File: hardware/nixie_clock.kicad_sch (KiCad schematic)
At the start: 0 parts

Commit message: Update.
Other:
- sheet driver_3_digits_1_dot_right: file driver_3_digits_1_dot.kicad_sch -> driver_3_digits_1_dot_right.kicad_sch

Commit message: Add HT psu.
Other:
- sheet driver_3_digits_1_dot_left ports: added 170V_INTERN; removed none
- sheet power_supply ports: added 170V_INTERN; removed none
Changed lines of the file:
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@@
+	(wire
+		(pts
+			(xy 106.68 130.81) (xy 106.68 137.16)
+		)
+		(stroke
+			(width 0)
+			(type default)
+		)
+	)
 	(wire
 		(pts
@@
 	(wire
 		(pts
+			(xy 147.32 137.16) (xy 147.32 53.34)
+		)
+		(stroke
+			(width 0)
+			(type default)
+		)
+	)
+	(wire
+		(pts
 			(xy 163.83 128.27) (xy 167.64 128.27)
 		)
@@
 	(wire
 		(pts
+			(xy 147.32 53.34) (xy 142.24 53.34)
+		)
+		(stroke
+			(width 0)
+			(type default)
+		)
+	)
+	(wire
+		(pts
+			(xy 106.68 137.16) (xy 147.32 137.16)
+		)
+		(stroke
+			(width 0)
+			(type default)
+		)
+	)
+	(wire
+		(pts
 			(xy 87.63 77.47) (xy 162.56 77.47)
 		)
@@
 		(pts
 			(xy 151.13 88.9) (xy 200.66 88.9)
+		)
+		(stroke
+			(width 0)
+			(type default)
+		)
+	)
+	(wire
+		(pts
+			(xy 109.22 130.81) (xy 106.68 130.81)
 		)
 		(stroke
@@
 			)
 		)
+		(pin "170V_INTERN" output
+			(at 142.24 53.34 0)
+			(effects
+				(font
+					(size 1.27 1.27)
+				)
+				(justify right)
+			)
+		)
 		(instances
 			(project "nixie_clock"
@@
 			(effects
 				(font
+					(size 1.27 1.27)
+				)
+				(justify left)
+			)
+		)
+		(pin "170V_INTERN" input
+			(at 109.22 130.81 180)
+			(effects
+				(font

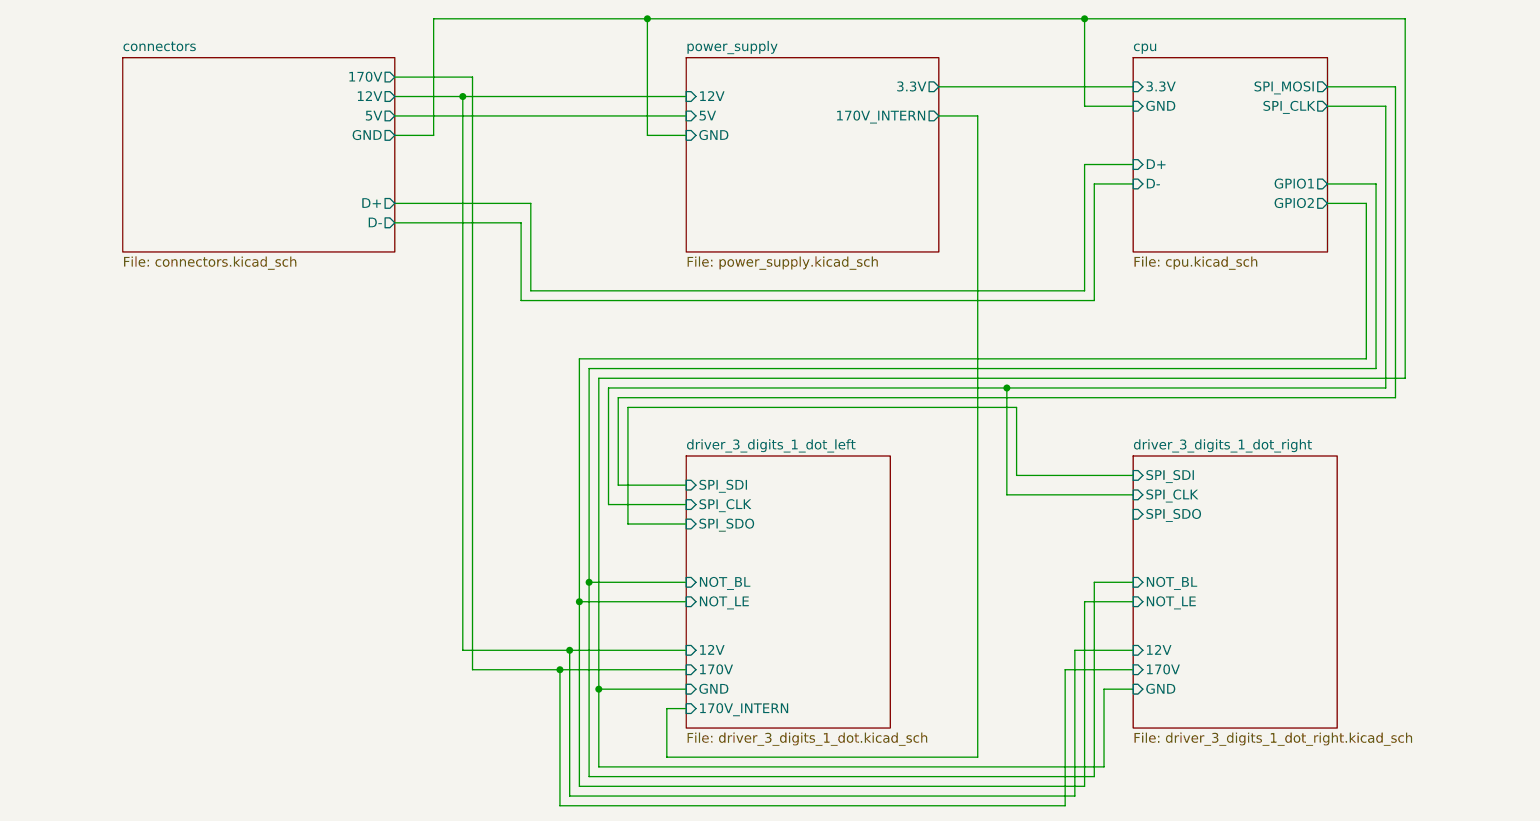
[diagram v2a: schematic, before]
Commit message: Fix most of ERC on schema. Add missing wire on RV1. Add PWR_FLG on GND to avoid error. Add resistor for unused SPI_OUT of HV5622. Add PTC on 3v3 supply.
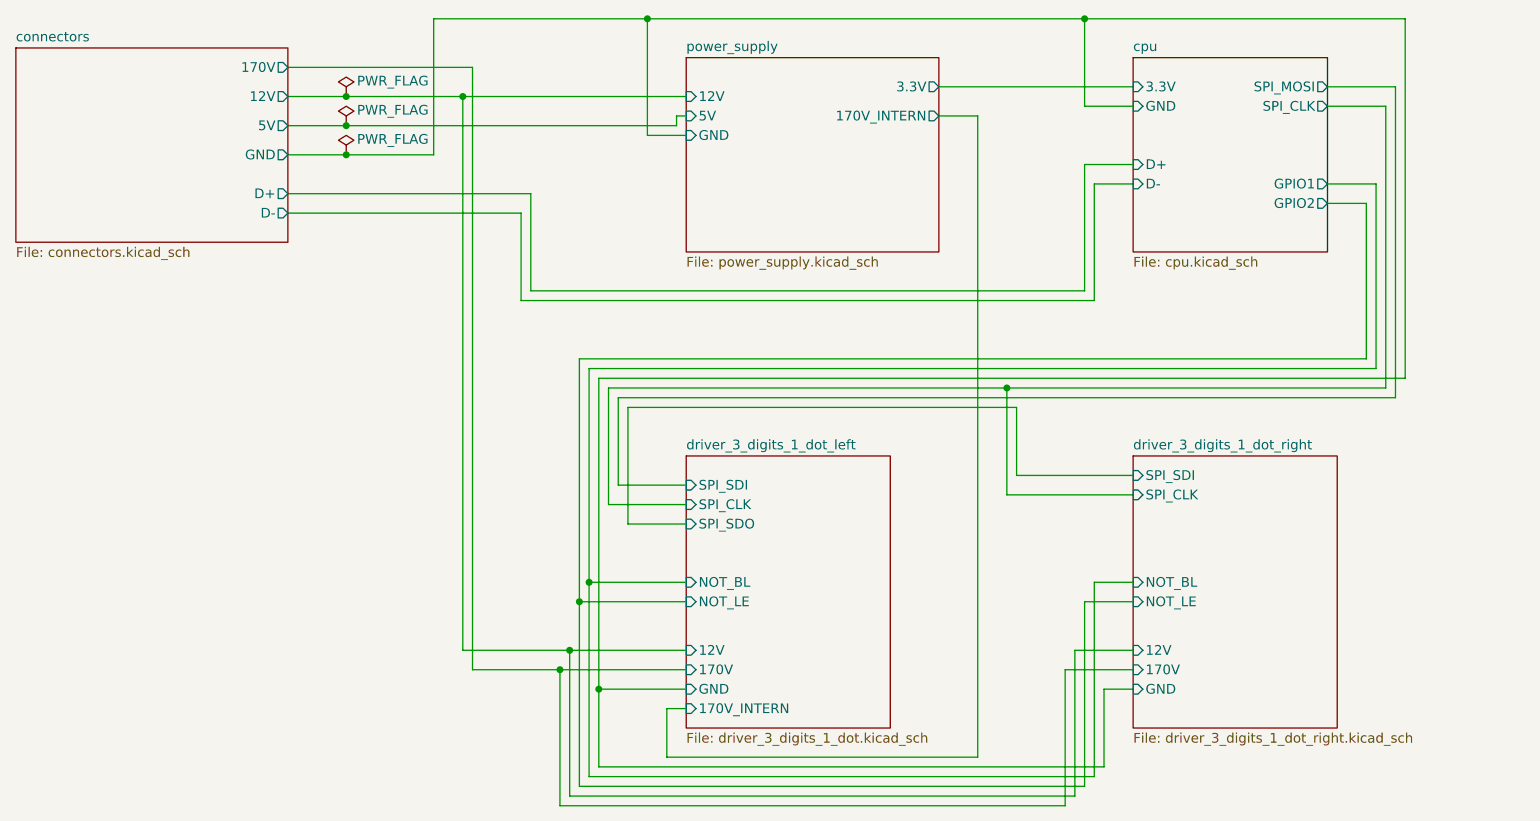
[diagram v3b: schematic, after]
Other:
- sheet driver_3_digits_1_dot_right ports: added none; removed SPI_SDO
